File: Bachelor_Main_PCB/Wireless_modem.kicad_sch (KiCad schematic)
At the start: 59 parts, among them J10 JAE_SIM_Card_SF72S006, J12 M20-9990245, J18 CONMHF1-SMD-G-T, J19 CONMHF1-SMD-G-T, J20 CONMHF1-SMD-G-T, Q1 SSM3J358R,LF, Q10 NX3008NBKW, Q11 NX3008NBKW, Q5 NX3008NBKW, Q6 NX3008NBKW, Q7 NX3008NBKW, Q8 NX3008NBKW, Q9 NX3008NBKW, U2 RC7620_1104627, U5 ESD7004MUTAG

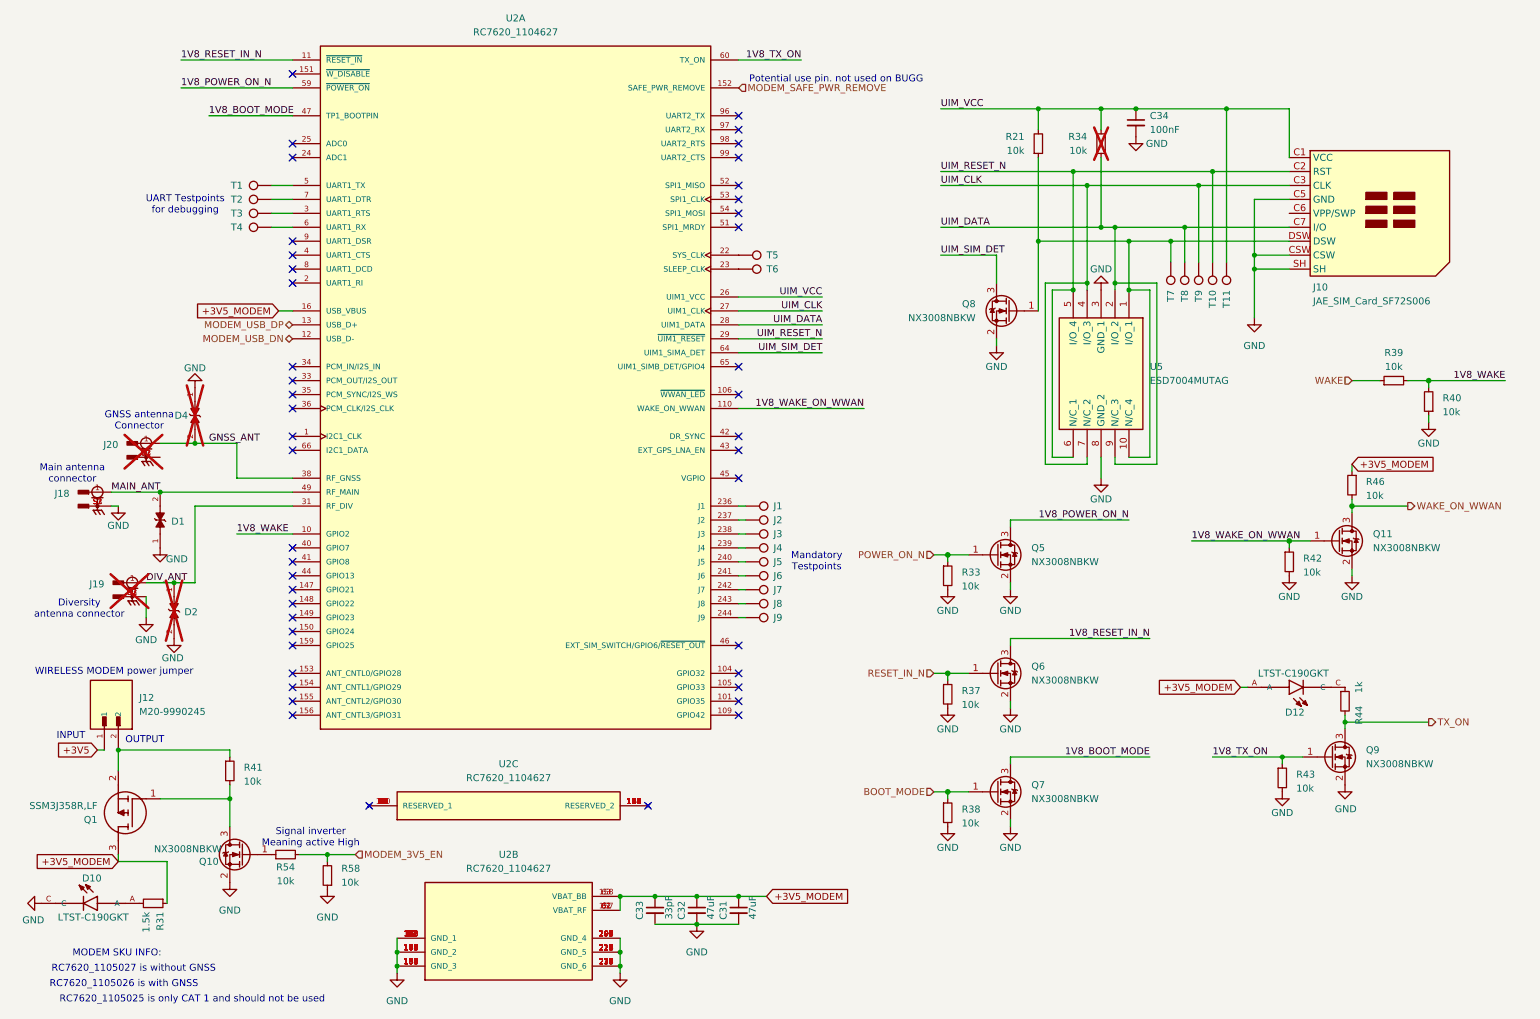
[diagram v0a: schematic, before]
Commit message: Fixed DRC, footprints and power flags and no-connect flags
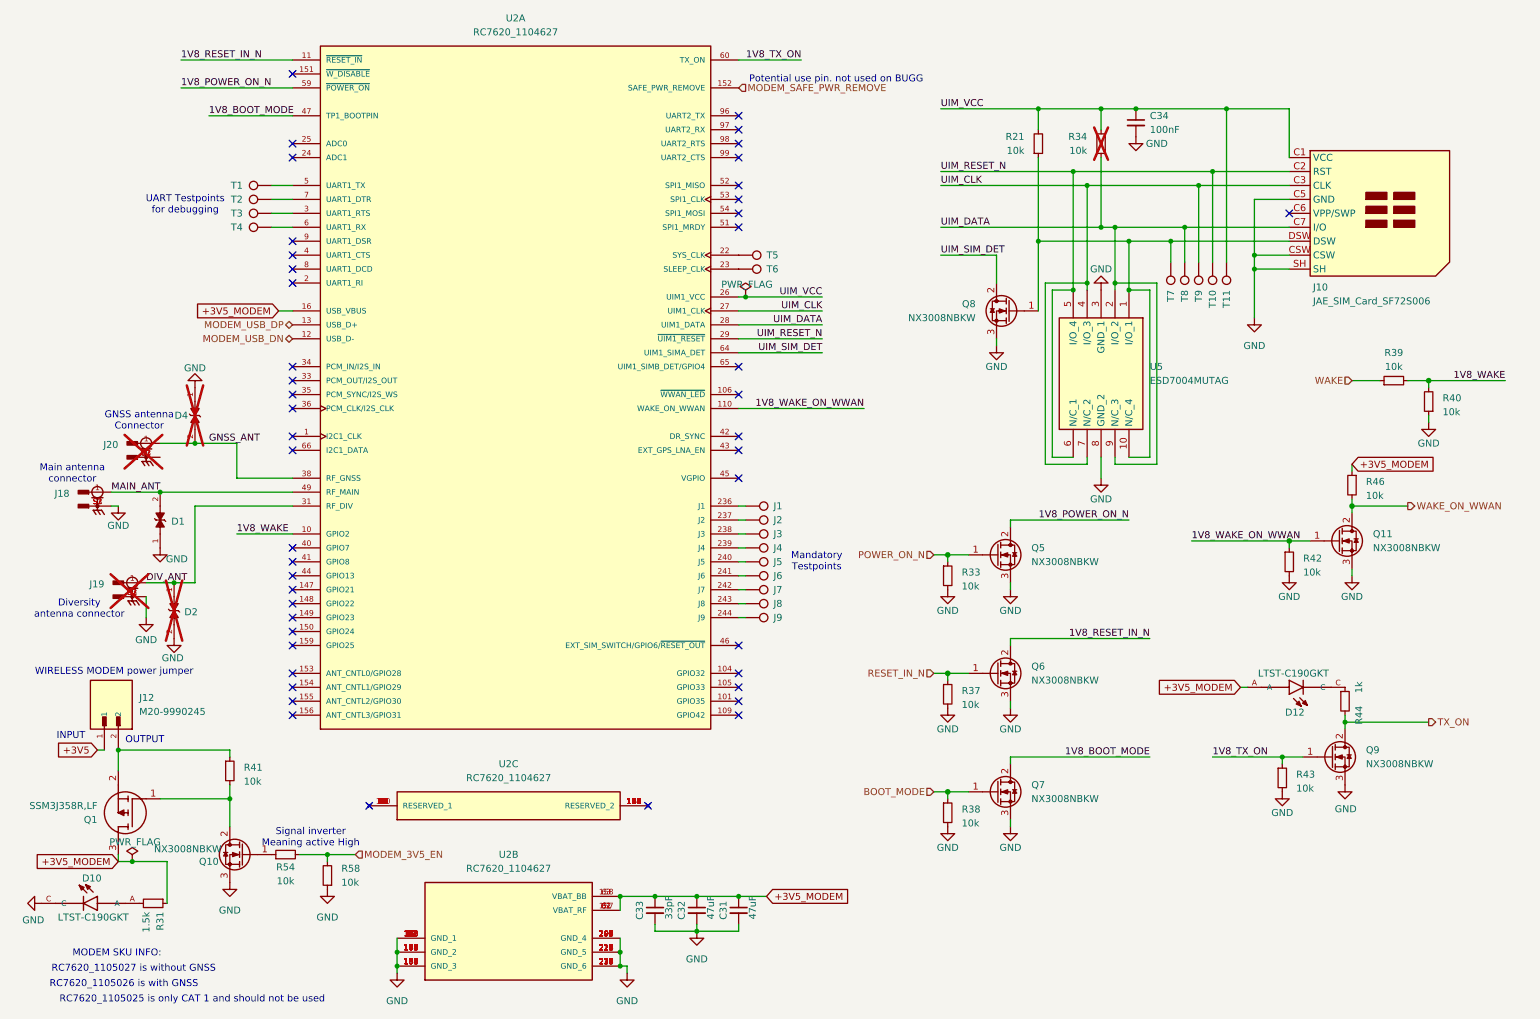
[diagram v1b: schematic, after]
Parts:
- Q10, Q11, Q5, Q6, Q7, Q8, Q9: symbol Device:Q_NMOS_GSD -> Transistor_FET:Q_NMOS_GDS
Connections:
- net 1V8_BOOT_MODE: now also Q7.2 (D); no longer Q7.3 (D)
- net 1V8_POWER_ON_N: now also Q5.2 (D); no longer Q5.3 (D)
- net 1V8_RESET_IN_N: now also Q6.2 (D); no longer Q6.3 (D)
- net GND: now also Q10.3 (S), Q11.3 (S), Q5.3 (S), Q6.3 (S), Q7.3 (S), Q8.3 (S), Q9.3 (S); no longer Q10.2 (S), Q11.2 (S), Q5.2 (S), Q6.2 (S), Q7.2 (S), Q8.2 (S), Q9.2 (S)
- net TX_ON: now also Q9.2 (D); no longer Q9.3 (D)
- net UIM_SIM_DET: now also Q8.2 (D); no longer Q8.3 (D)
- net WAKE_ON_WWAN: now also Q11.2 (D); no longer Q11.3 (D)
- net at Q1.1 (G), R41.2: now also Q10.2 (D); no longer Q10.3 (D)
- no-connect marks 45 -> 46

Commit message: Removed Modem_safe_PWR_remove pin.
was potential use for the MCU but would require level shifters and would not add any functionality ass the RPI controls the Modem anyway.
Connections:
- net MODEM_SAFE_PWR_REMOVE: no longer names the net of U2.152 (SAFE_PWR_REMOVE)
- no-connect marks 46 -> 45
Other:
- note removed: "Potential use pin. not used on BUGG"
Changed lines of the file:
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@@
-		)
-	)
-	(text "Potential use pin. not used on BUGG"
-		(exclude_from_sim no)
-		(at 161.29 27.686 0)
-		(effects
-			(font
-				(size 1.27 1.27)
-			)
 		)
 	)
@@
 	)
 	(no_connect
-		(at 127 160.02)
-	)
-	(no_connect
 		(at 143.51 138.43)
 	)
@@
 	)
 	(no_connect
+		(at 143.51 29.21)
+	)
+	(no_connect
 		(at 62.23 85.09)
-	)
-	(no_connect
-		(at 76.2 160.02)
 	)
 	(no_connect
@@
 		(effects
 			(font
-				(size 1.27 1.27)
-			)
-			(justify left)
-		)
-	)
-	(hierarchical_label "MODEM_SAFE_PWR_REMOVE"
-		(shape input)
-		(at 143.51 29.21 0)
-		(effects
-			(font

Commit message: Fix all DRC errors and warnings
except not connected pins still unrouted to MCU
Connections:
- net GND: now also J20.S1, J20.S2, J20.S3
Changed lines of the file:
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@@
 	)
 	(junction
-		(at 121.92 189.23)
+		(at 123.19 189.23)
 		(diameter 0)
 		(color 0 0 0 0)
@@
 	)
 	(junction
-		(at 121.92 186.69)
+		(at 123.19 186.69)
 		(diameter 0)
 		(color 0 0 0 0)
@@
 	(wire
 		(pts
+			(xy 123.19 189.23) (xy 121.92 189.23)
+		)
+		(stroke
+			(width 0)
+			(type default)
+		)
+	)
+	(wire
+		(pts
 			(xy 128.27 176.53) (xy 135.89 176.53)
 		)
@@
 	(wire
 		(pts
+			(xy 135.89 185.42) (xy 135.89 182.88)
+		)
+		(stroke
+			(width 0)
+			(type default)
+		)
+	)
+	(wire
+		(pts
 			(xy 158.75 77.47) (xy 143.51 77.47)
 		)
@@
 	(wire
 		(pts
-			(xy 121.92 184.15) (xy 121.92 186.69)
+			(xy 123.19 184.15) (xy 123.19 186.69)
 		)
 		(stroke
@@
 	(wire
 		(pts
-			(xy 180.34 59.69) (xy 190.5 59.69)
+			(xy 123.19 184.15) (xy 121.92 184.15)
 		)
 		(stroke
@@
 	(wire
 		(pts
-			(xy 81.28 186.69) (xy 81.28 189.23)
+			(xy 180.34 59.69) (xy 190.5 59.69)
 		)
 		(stroke
@@
 	(wire
 		(pts
-			(xy 237.49 59.69) (xy 243.84 59.69)
+			(xy 81.28 186.69) (xy 81.28 189.23)
 		)
 		(stroke
@@
 	(wire
 		(pts
-			(xy 207.01 96.52) (xy 207.01 97.79)
+			(xy 237.49 59.69) (xy 243.84 59.69)
 		)
 		(stroke
@@
 	(wire
 		(pts
-			(xy 215.9 33.02) (xy 232.41 33.02)
+			(xy 207.01 96.52) (xy 207.01 97.79)
 		)
 		(stroke
@@
 	(wire
 		(pts
-			(xy 123.19 189.23) (xy 121.92 189.23)
+			(xy 215.9 33.02) (xy 232.41 33.02)
 		)
 		(stroke
@@
 	(wire
 		(pts
-			(xy 121.92 186.69) (xy 121.92 189.23)
+			(xy 123.19 186.69) (xy 123.19 189.23)
 		)
 		(stroke
@@
 	(wire
 		(pts
+			(xy 123.19 186.69) (xy 121.92 186.69)
+		)
+		(stroke
+			(width 0)
+			(type default)
+		)
+	)
+	(wire
+		(pts
 			(xy 237.49 62.23) (xy 237.49 71.12)
 		)
@@
 	(symbol
 		(lib_id "power:GND")
-		(at 135.89 182.88 0)
+		(at 135.89 185.42 0)
 		(unit 1)
 		(exclude_from_sim no)
@@
 		(fields_autoplaced yes)
 		(property "Reference" "#PWR01"
-			(at 135.89 189.23 0)
+			(at 135.89 191.77 0)
 			(effects
 				(font
@@
 		)
 		(property "Value" "GND"
-			(at 135.89 187.96 0)
+			(at 135.89 190.5 0)
 			(effects
 				(font
@@
 		)
 		(property "Footprint" ""
-			(at 135.89 182.88 0)
+			(at 135.89 185.42 0)
 			(effects
 				(font
@@
 		)
 		(property "Datasheet" ""
-			(at 135.89 182.88 0)
+			(at 135.89 185.42 0)
 			(effects
 				(font
@@
 		)
 		(property "Description" "Power symbol creates a global label with name \"GND\" , ground"
-			(at 135.89 182.88 0)
+			(at 135.89 185.42 0)
 			(effects
 				(font
@@
 					(unit 1)
 				)
+			)
+		)
+	)
+	(symbol
+		(lib_id "power:GND")
+		(at 38.1 96.52 0)
+		(unit 1)
+		(exclude_from_sim no)
+		(in_bom yes)
+		(on_board yes)
+		(dnp no)
+		(property "Reference" "#PWR092"
+			(at 38.1 102.87 0)
+			(effects
+				(font
+					(size 1.27 1.27)
+				)
+				(hide yes)
+			)
+		)
+		(property "Value" "GND"
+			(at 38.1 100.076 0)
+			(effects
+				(font
+					(size 1.27 1.27)
+				)
+			)
+		)
+		(property "Footprint" ""
+			(at 38.1 96.52 0)
+			(effects
+				(font
+					(size 1.27 1.27)
+				)
+				(hide yes)
+			)
+		)
+		(property "Datasheet" ""
+			(at 38.1 96.52 0)
+			(effects
+				(font
+					(size 1.27 1.27)
+				)
+				(hide yes)
+			)
+		)
+		(property "Description" "Power symbol creates a global label with name \"GND\" , ground"
+			(at 38.1 96.52 0)
+			(effects
+				(font
+					(size 1.27 1.27)
+				)
+				(hide yes)
+			)
+		)
+		(pin "1"
+		)
+		(instances
+			(project "Bachelor_Main_PCB"
+				(path "/3544d663-329e-4884-b753-28436ca187e8/0bbef2a3-1d79-4cf0-b531-d6abf690b331"
+					(reference "#PWR092")
+					(unit 1)
+				)

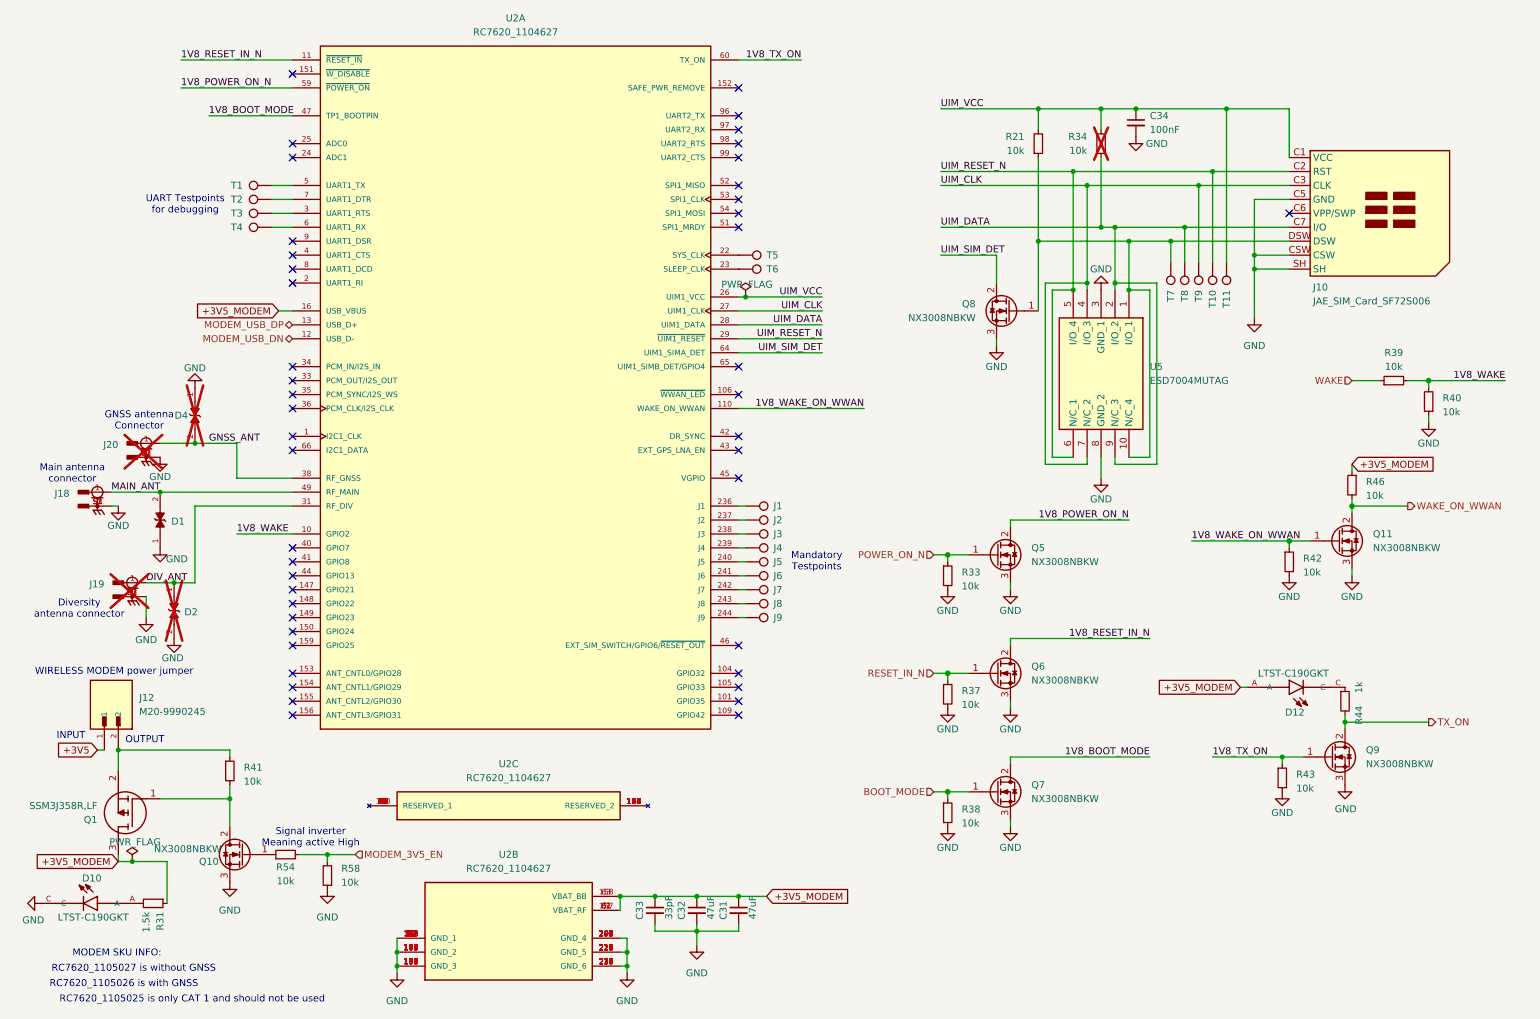
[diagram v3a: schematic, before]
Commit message: Imported components from schematic to PCB and Reanotat all designators
THis means every designator is now different and the references made prior no longer applies
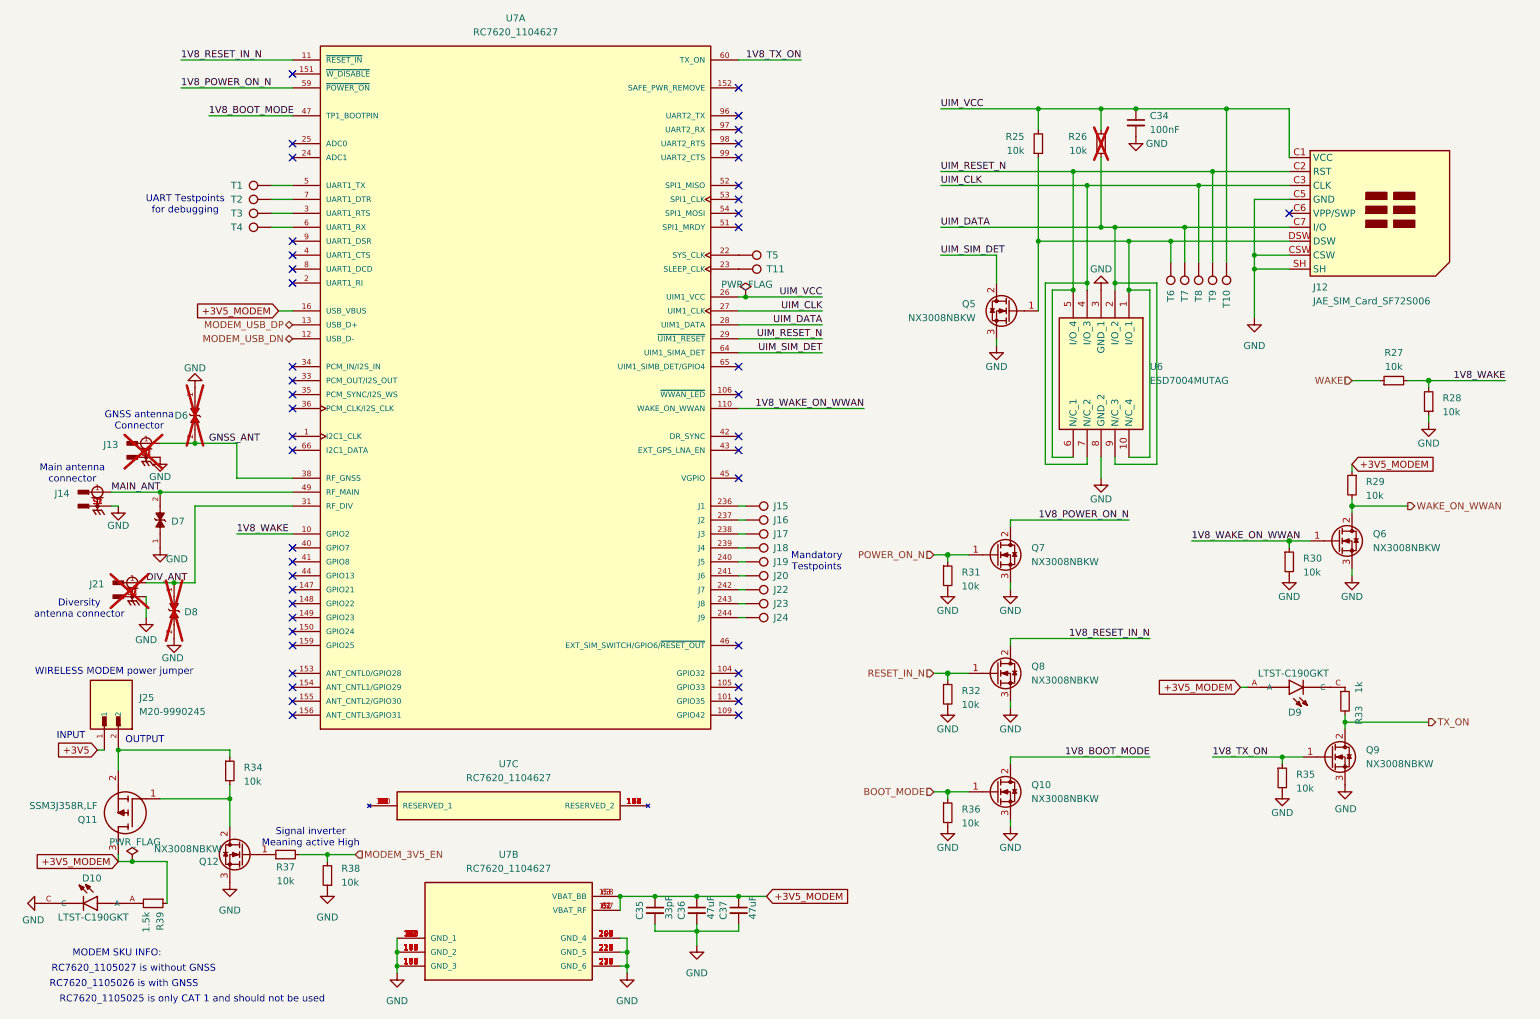
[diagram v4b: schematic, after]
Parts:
- renumbered C33 to C35, C32 to C36, C31 to C37, D4 to D6, D1 to D7, D2 to D8, D12 to D9, J10 to J12, J20 to J13, J18 to J14, J1 to J15, J2 to J16, J3 to J17, J4 to J18, J5 to J19, J6 to J20, J19 to J21, J7 to J22, J8 to J23, J9 to J24, J12 to J25, Q7 to Q10, Q1 to Q11, Q10 to Q12, Q8 to Q5, Q11 to Q6, Q5 to Q7, Q6 to Q8, R21 to R25, R34 to R26, R39 to R27, R40 to R28, R46 to R29, R42 to R30, R33 to R31, R37 to R32, R44 to R33, R41 to R34, R43 to R35, R38 to R36, R54 to R37, R58 to R38, R31 to R39, T11 to T10, T6 to T11, T7 to T6, T8 to T7, T9 to T8, T10 to T9, U5 to U6, U2 to U7

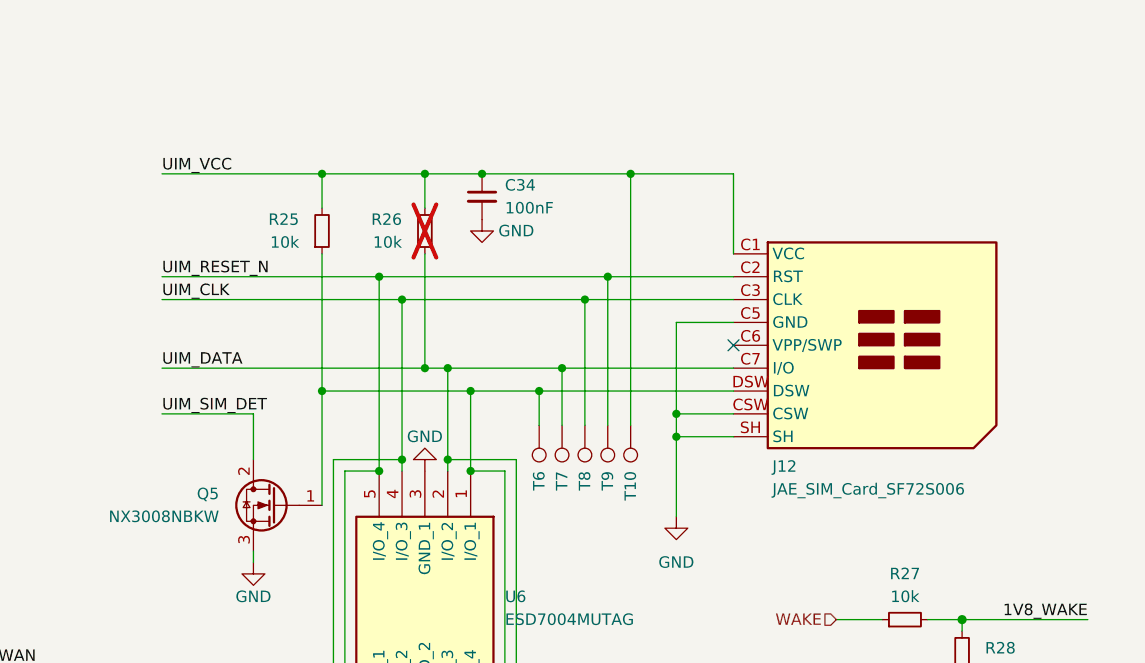
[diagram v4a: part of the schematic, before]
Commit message: Changed SIM card connector to SF70S006VBAR2000
the other one was not available
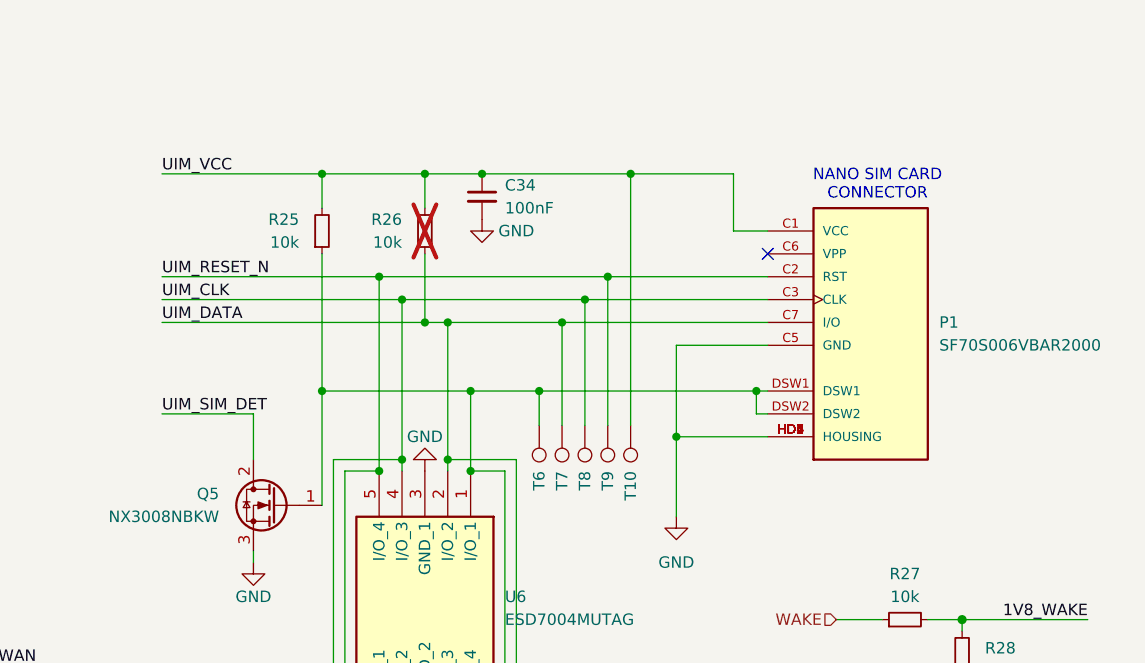
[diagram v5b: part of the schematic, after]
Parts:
- removed J12: JAE_SIM_Card_SF72S006, Connector_JAE:JAE_SIM_Card_SF72S006, symbol Connector:JAE_SIM_Card_SF72S006
- added P1: SF70S006VBAR2000, SF70S006VBAR2000:JAE_SF70S006VBAR2000, symbol SF70S006VBAR2000:SF70S006VBAR2000
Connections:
- net GND: now also P1.C5 (GND), P1.HD1 (HOUSING), P1.HD2 (HOUSING), P1.HD3 (HOUSING), P1.HD4 (HOUSING), P1.HD5 (HOUSING), P1.HD6 (HOUSING), P1.HD7 (HOUSING)
- net UIM_CLK: now also P1.C3 (CLK)
- net UIM_DATA: now also P1.C7 (I/O)
- net UIM_RESET_N: now also P1.C2 (RST)
- net UIM_VCC: now also P1.C1 (VCC)
- net at Q5.1 (G), R25.1, T6.1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: now also P1.DSW1, P1.DSW2
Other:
- note added: "NANO SIM CARD CONNECTOR"
